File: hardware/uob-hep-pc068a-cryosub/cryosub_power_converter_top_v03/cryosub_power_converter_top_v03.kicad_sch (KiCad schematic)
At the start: 11 parts, among them J1 Conn_02x04_Odd_Even, J2 Conn_02x05_Odd_Even, U1 LT3042xMSE

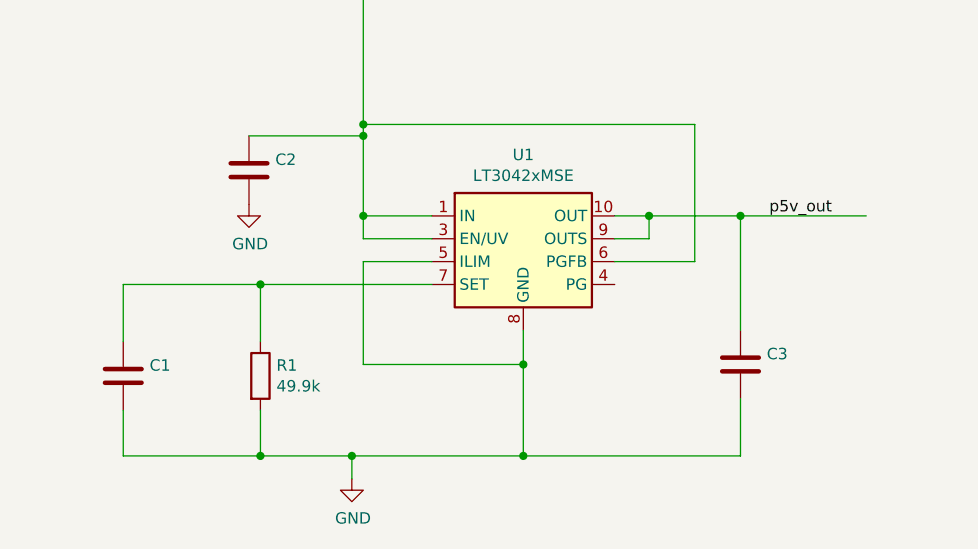
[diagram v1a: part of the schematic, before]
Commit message: Replacing FDD306 with SiS407
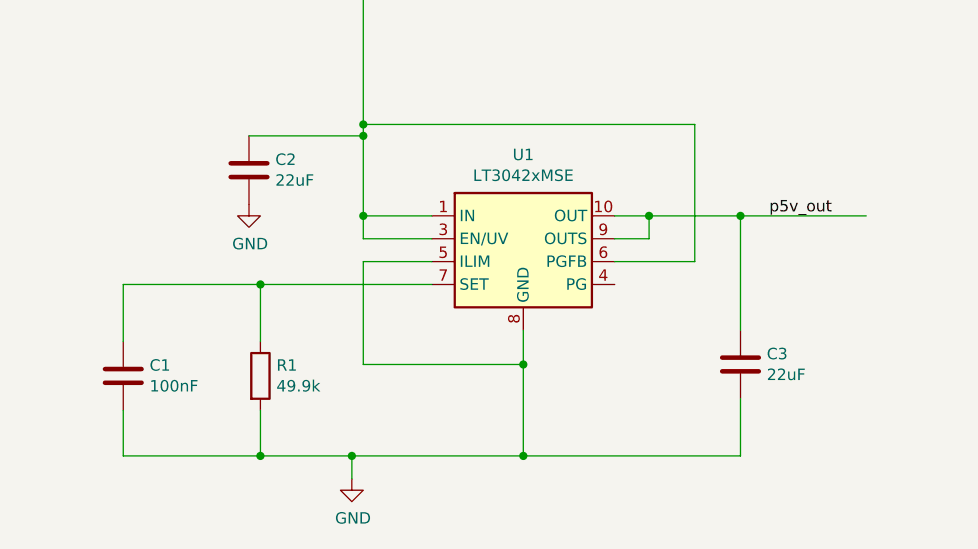
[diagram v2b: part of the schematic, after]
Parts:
- C1: value (none) -> 100nF; footprint (none) -> Capacitor_SMD:C_0603_1608Metric
- C2, C3: value (none) -> 22uF; footprint (none) -> Capacitor_SMD:C_0805_2012Metric_Pad1.18x1.45mm_HandSolder
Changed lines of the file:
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@@
       (effects (font (size 1.27 1.27)) (justify left))
     )
-    (property "Value" "" (id 1) (at 33.401 177.673 0)
-      (effects (font (size 1.27 1.27)) (justify left))
-    )
-    (property "Footprint" "" (id 2) (at 31.4452 180.34 0)
+    (property "Value" "100nF" (id 1) (at 33.401 177.673 0)
+      (effects (font (size 1.27 1.27)) (justify left))
+    )
+    (property "Footprint" "Capacitor_SMD:C_0603_1608Metric" (id 2) (at 31.4452 180.34 0)
       (effects (font (size 1.27 1.27)) hide)
     )
@@
       (effects (font (size 1.27 1.27)) (justify left))
     )
-    (property "Value" "" (id 1) (at 101.981 176.403 0)
-      (effects (font (size 1.27 1.27)) (justify left))
-    )
-    (property "Footprint" "" (id 2) (at 100.0252 179.07 0)
+    (property "Value" "22uF" (id 1) (at 101.981 176.403 0)
+      (effects (font (size 1.27 1.27)) (justify left))
+    )
+    (property "Footprint" "Capacitor_SMD:C_0805_2012Metric_Pad1.18x1.45mm_HandSolder" (id 2) (at 100.0252 179.07 0)
       (effects (font (size 1.27 1.27)) hide)
     )
@@
       (effects (font (size 1.27 1.27)) (justify left))
     )
-    (property "Value" "" (id 1) (at 47.371 154.813 0)
-      (effects (font (size 1.27 1.27)) (justify left))
-    )
-    (property "Footprint" "" (id 2) (at 45.4152 157.48 0)
+    (property "Value" "22uF" (id 1) (at 47.371 154.813 0)
+      (effects (font (size 1.27 1.27)) (justify left))
+    )
+    (property "Footprint" "Capacitor_SMD:C_0805_2012Metric_Pad1.18x1.45mm_HandSolder" (id 2) (at 45.4152 157.48 0)
       (effects (font (size 1.27 1.27)) hide)
     )
@@
       (reference "Q2") (unit 1) (value "IRLML2402TRPBF") (footprint "Package_TO_SOT_SMD:SOT-23")
     )
-    (path "/00000000-0000-0000-0000-000061394019/00000000-0000-0000-0000-000060855e74"
-      (reference "Q3") (unit 1) (value "AOD413A") (footprint "Package_TO_SOT_SMD:TO-252-3_TabPin2")
+    (path "/00000000-0000-0000-0000-000061394019/16cd4310-7f18-46c4-bffc-83ac4a1b5ca2"
+      (reference "Q?") (unit 1) (value "SiS407DN") (footprint "Package_SO:Vishay_PowerPAK_1212-8_Single")
     )
     (path "/00000000-0000-0000-0000-0000613f83d0"
